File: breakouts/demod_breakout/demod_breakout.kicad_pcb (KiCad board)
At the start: 2 copper layers, 31 parts, among them P1 CONN_02X03, P2 CONN_01X02, U1 CONN_SMA, U2 mounting_box, U3 TCM-63AX+, U4 ADL5380, U5 TCM-63AX+, U6 CONN_SMA, U7 ADM7150

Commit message: demod component placement
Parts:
- added C21: 100 nF, Capacitors_SMD:C_0402, F.Cu at (91.0, 134.8)
- added C22: 100 nF, Capacitors_SMD:C_0402, F.Cu at (95.5, 110.0)
- added C23: 100 nF, Capacitors_SMD:C_0402, F.Cu at (93.2, 141.2)
- added C24: 100 nF, Capacitors_SMD:C_0402, F.Cu at (90.8, 102.0)
- added C25: DNP, Capacitors_SMD:C_0402, F.Cu at (96.2, 136.8)
- added C26: 100 nF, Capacitors_SMD:C_0402, F.Cu at (96.8, 141.8)
- added C27: DNP, Capacitors_SMD:C_0402, F.Cu at (88.2, 104.8)
- added C28: 100 nF, Capacitors_SMD:C_0402, F.Cu at (97.0, 105.5)
- added C29: 100 nF, Capacitors_SMD:C_0402, F.Cu at (103.8, 136.5)
- added C30: 100 nF, Capacitors_SMD:C_0402, F.Cu at (99.2, 98.0)
- added C31: 100 nF, Capacitors_SMD:C_0402, F.Cu at (104.8, 123.5)
- added C32: 100 nF, Capacitors_SMD:C_0402, F.Cu at (98.5, 131.0)
- added P3: CONN_02X03, Pin_Headers:Pin_Header_Straight_2x03, F.Cu at (111.5, 120.8)
- added P5: CONN_01X02, Pin_Headers:Pin_Header_Straight_1x02, F.Cu at (103.2, 127.8)
- added R10: 604, Resistors_SMD:R_0402, F.Cu at (90.2, 104.5)
- added R11: 604, Resistors_SMD:R_0402, F.Cu at (101.2, 136.8)
- added R12: 604, Resistors_SMD:R_0402, F.Cu at (95.8, 98.0)
- added R13: 0, Resistors_SMD:R_0402, F.Cu at (92.2, 138.8)
- added R14: 0, Resistors_SMD:R_0402, F.Cu at (90.2, 107.5)
- added R3: 10k, Resistors_SMD:R_0402, F.Cu at (89.2, 134.8)
- added R4: 10k, Resistors_SMD:R_0402, F.Cu at (95.2, 108.2)
- added R5: 10k, Resistors_SMD:R_0402, F.Cu at (91.2, 140.8)
- added R6: 10k, Resistors_SMD:R_0402, F.Cu at (92.5, 108.2)
- added R7: 604, Resistors_SMD:R_0402, F.Cu at (92.2, 136.8)
- added R8: 604, Resistors_SMD:R_0402, F.Cu at (88.2, 107.5)
- added R9: 604, Resistors_SMD:R_0402, F.Cu at (96.2, 138.8)
- added U10: LT1567, Housings_SSOP:MSOP-8_3x3mm_Pitch0.65mm, F.Cu at (101.2, 139.8)
- added U11: LT1567, Housings_SSOP:MSOP-8_3x3mm_Pitch0.65mm, F.Cu at (96.2, 101.0)
- added U12: CONN_SMA, vna_footprints:732512200_SMA, F.Cu at (111.2, 139.0)
- added U13: CONN_SMA, vna_footprints:732512200_SMA, F.Cu at (107.2, 100.0)
- added U14: LD1117S12CTR, TO_SOT_Packages_SMD:SOT-23, F.Cu at (98.2, 127.8)
- added U8: LTC1566-1, Housings_SOIC:SOIC-8_3.9x4.9mm_Pitch1.27mm, F.Cu at (91.0, 129.0)
- added U9: LTC1566-1, Housings_SOIC:SOIC-8_3.9x4.9mm_Pitch1.27mm, F.Cu at (91.0, 113.2)
- C6: footprint Capacitors_SMD:C_0603 -> Capacitors_SMD:C_0402
- moved U2 104.8 mm to (230.2, 39.5)
- moved U6 73.8 mm to (83.5, 140.0), turned to 90 degrees
- moved C3 72.0 mm to (78.5, 122.0), turned to 90 degrees
- moved C13 71.2 mm to (83.5, 134.0), turned to 270 degrees
- moved C5 70.6 mm to (80.0, 122.0), turned to 90 degrees
- moved U5 69.5 mm to (83.5, 129.5), turned to 180 degrees
- moved C9 68.5 mm to (83.0, 125.0), turned to 270 degrees
- moved C4 67.9 mm to (81.5, 116.0)
- moved C2 67.6 mm to (81.5, 114.0)
- moved C8 67.1 mm to (84.5, 125.0), turned to 270 degrees
- moved U4 66.5 mm to (83.8, 120.0)
- moved C6 65.6 mm to (83.5, 113.5), turned to 90 degrees
- moved U1 65.4 mm to (83.5, 98.0), turned to 270 degrees
- moved U3 65.1 mm to (83.5, 108.5)
- moved C1 65.0 mm to (83.5, 104.0), turned to 90 degrees
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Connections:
- P1 pad 1: /BRF_IN -> /ILO_ADL
- P1 pad 2: /BRF_IP -> /IHI_ADL
- P1 pad 5: /BRF_QN -> /QLO_ADL
- P1 pad 6: /BRF_QP -> /QHI_ADL
- U4 pad 21: Net-(C6-Pad1) -> Net-(C7-Pad1)
- U4 pad 22: Net-(C7-Pad1) -> Net-(C6-Pad1)
- U5 pad 2: GND -> Net-(C13-Pad1)
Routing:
- net GND: track 0.00 -> 25.6 mm, vias 0 -> 11
- net +5V: track 0.00 -> 11.0 mm
- net Net-(C1-Pad2): track 0.00 -> 5.45 mm
- net Net-(C13-Pad2): track 0.00 -> 5.45 mm
- net Net-(C7-Pad1): track 0.00 -> 4.41 mm
- net Net-(C6-Pad1): track 0.00 -> 4.00 mm
- net Net-(C6-Pad2): track 0.00 -> 3.39 mm
- net Net-(C7-Pad2): track 0.00 -> 2.96 mm
- net Net-(C9-Pad1): track 0.00 -> 2.71 mm
- net Net-(C8-Pad1): track 0.00 -> 2.71 mm
- net Net-(C9-Pad2): track 0.00 -> 2.68 mm
- net Net-(C8-Pad2): track 0.00 -> 2.47 mm
- net Net-(C1-Pad1): track 0.00 -> 2.36 mm
- net Net-(C13-Pad1): track 0.00 -> 2.36 mm
- added copper zone on In1.Cu, net GND
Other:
- board outline added: 40.8 x 50 mm
- copper layers 2 -> 4

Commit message: layout of demod board
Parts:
- moved P3 10.1 mm to (107.0, 129.8), turned to 180 degrees
- moved C30 10.0 mm to (89.2, 98.0)
- moved C20 9.20 mm to (108.5, 110.8)
- moved U7 9.02 mm to (103.8, 109.2)
- moved C18 8.84 mm to (107.0, 110.8)
- moved R2 8.84 mm to (107.0, 108.2)
- moved C19 8.66 mm to (106.5, 105.0)
- moved C12 8.55 mm to (100.0, 108.8)
- moved C14 8.38 mm to (99.2, 105.5)
- moved C15 8.36 mm to (98.2, 108.8)
- moved C17 8.05 mm to (100.2, 111.8)
- moved C16 7.97 mm to (102.5, 105.0)
- moved P5 7.81 mm to (104.2, 120.0), turned to 90 degrees
- moved C29 6.27 mm to (97.5, 137.0), turned to 0 degrees
- moved U12 6.05 mm to (105.2, 139.8), turned to 90 degrees
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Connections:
- P2 pad 1: Net-(C19-Pad2) -> GND
- P2 pad 2: GND -> Net-(C19-Pad2)
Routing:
- net /QHI_ADL: track 0.00 -> 18.8 mm
- net /QLO_ADL: track 0.00 -> 18.8 mm
- net /IHI_ADL: track 0.00 -> 13.5 mm, vias 0 -> 1
- net /ILO_ADL: track 0.00 -> 8.82 mm, vias 0 -> 1
- net Net-(C22-Pad1): track 0.00 -> 5.93 mm
- net Net-(C21-Pad1): track 0.00 -> 5.93 mm
- net GND: track 25.6 -> 30.0 mm, vias 11 -> 14
- net Net-(R1-Pad2): track 0.00 -> 1.78 mm
- net +5V: track 11.0 -> 11.8 mm, vias 0 -> 1
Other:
- board size 40.8 x 50 mm -> 33.8 x 50.2 mm

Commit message: layout of if processing on demodo board..
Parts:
- moved P5 9.52 mm to (106.5, 129.2), turned to 270 degrees
- moved C24 7.62 mm to (92.5, 107.2), turned to 270 degrees
- moved P3 6.52 mm to (106.5, 123.2)
- moved C31 5.01 mm to (99.8, 131.0), turned to 90 degrees
- moved R12 4.14 mm to (90.0, 101.0), turned to 270 degrees
- moved C30 3.40 mm to (92.0, 96.0), turned to 270 degrees
- moved R11 3.34 mm to (96.8, 138.0), turned to 180 degrees
- moved U14 3.34 mm to (97.0, 131.5)
- moved R5 3.26 mm to (89.8, 136.8), turned to 180 degrees
- moved C32 3.09 mm to (97.0, 134.2)
- moved C23 3.04 mm to (89.5, 138.2), turned to 0 degrees
- moved R9 2.69 mm to (94.5, 138.0), turned to 180 degrees
- moved C21 2.61 mm to (88.2, 135.0), turned to 180 degrees
- moved C27 2.37 mm to (89.0, 104.2), turned to 90 degrees
- moved R10 2.37 mm to (90.5, 104.2), turned to 90 degrees
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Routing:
- net /IOUT: track 0.00 -> 23.9 mm, vias 0 -> 1
- net +5V: track 11.8 -> 32.2 mm, vias 1 -> 7
- net /QOUT: track 0.00 -> 16.8 mm, vias 0 -> 1
- net /ILO_ADL: track 8.82 -> 21.9 mm, vias 1 -> 2
- net Net-(C27-Pad1): track 0.00 -> 12.9 mm
- net Net-(R13-Pad2): track 0.00 -> 12.2 mm, vias 0 -> 2
- net GND: track 30.0 -> 41.8 mm, vias 14 -> 26
- net Net-(C25-Pad1): track 0.00 -> 10.5 mm
- net /IHI_ADL: track 13.5 -> 23.8 mm, vias 1 -> 2
- net Net-(R14-Pad2): track 0.00 -> 9.76 mm, vias 0 -> 2
- net Net-(C22-Pad1): track 5.93 -> 11.8 mm
- net Net-(C21-Pad1): track 5.93 -> 11.8 mm
- net /VOUT_REF: track 0.00 -> 5.35 mm
- net Net-(R12-Pad1): track 0.00 -> 4.50 mm
- net Net-(R11-Pad1): track 0.00 -> 3.96 mm
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- added copper zone on In2.Cu, net +5V
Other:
- board text added: "IF I"
- board text added: "IF Q"
- board text added: "LO X dBm"
- board text added: "RF X dBm"
- board text added: "gnd 5v"
- board text added: "vref gnd"

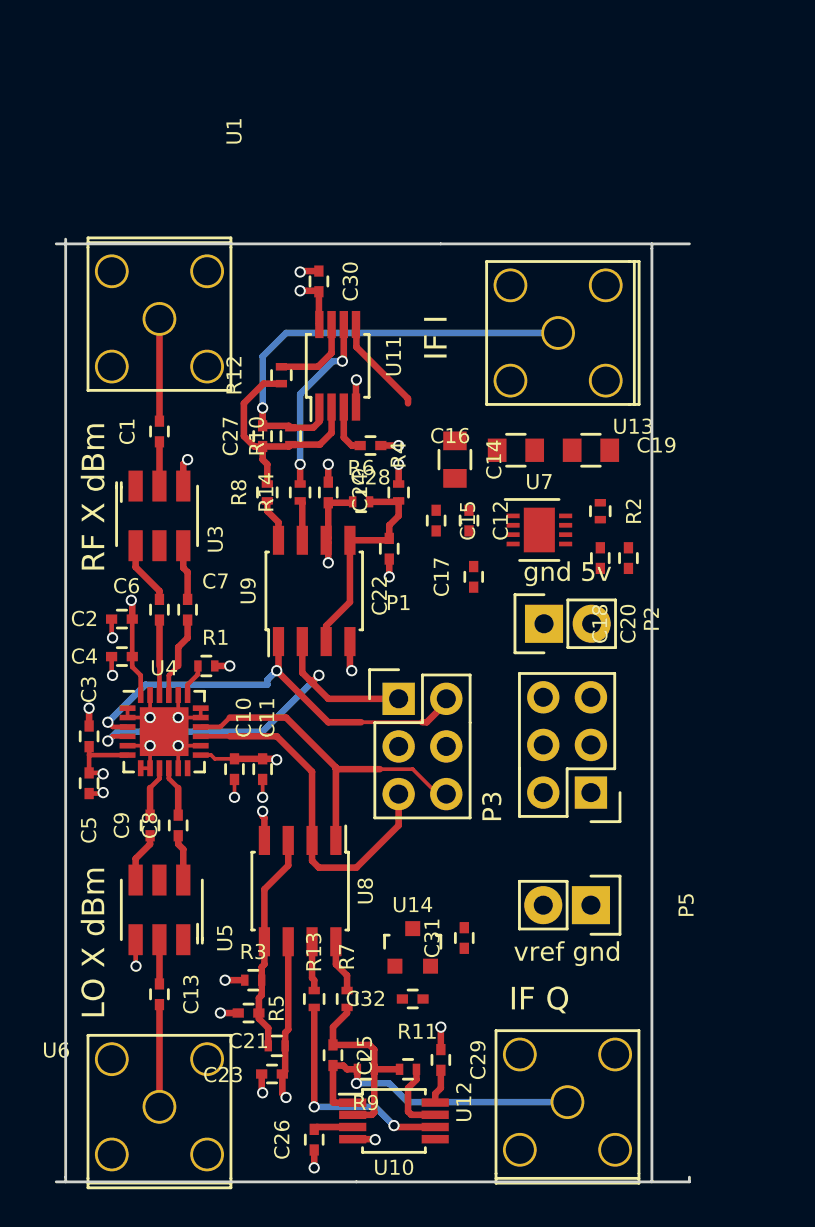
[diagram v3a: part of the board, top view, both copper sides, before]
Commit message: silkscreen cleanup on demod board
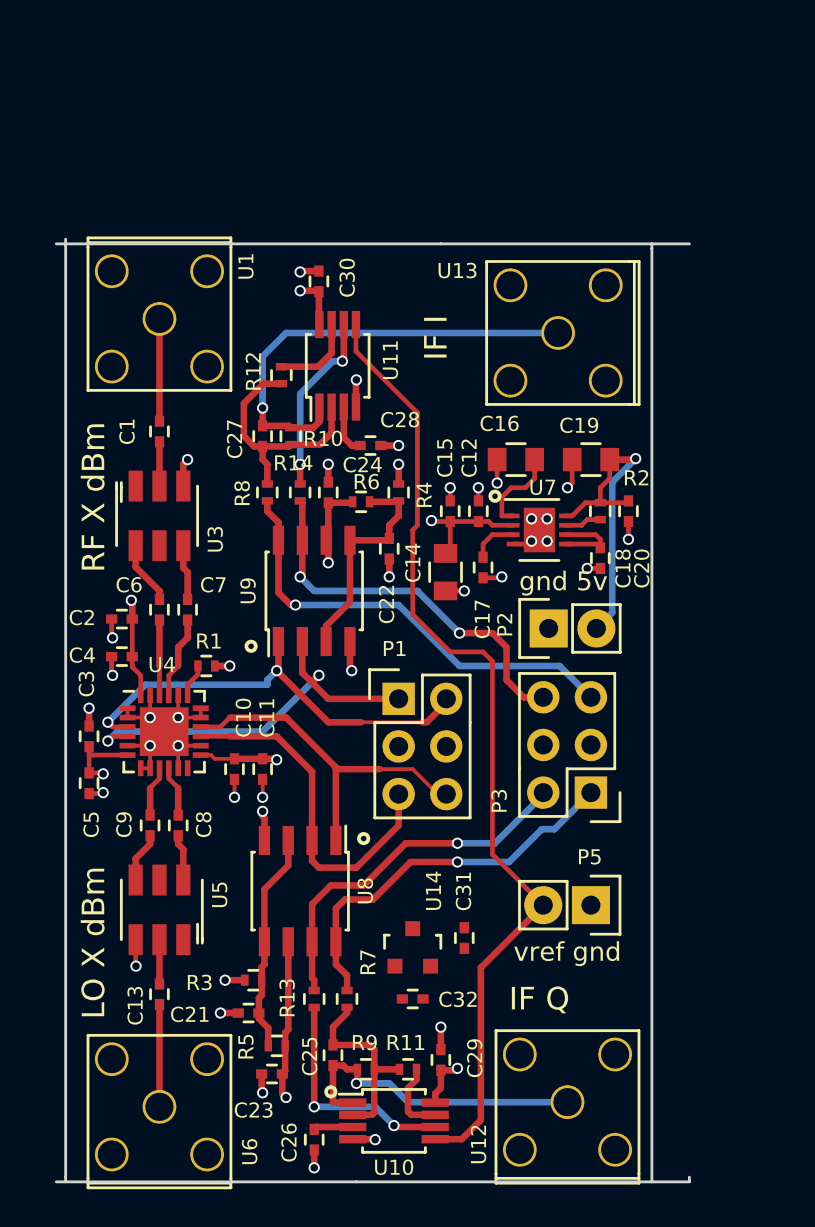
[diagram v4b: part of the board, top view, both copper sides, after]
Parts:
- moved C14 6.02 mm to (98.8, 111.5), turned to 90 degrees
- moved C20 2.50 mm to (108.5, 108.2)
- moved C15 0.90 mm to (99.0, 108.2)
- moved C12 0.71 mm to (100.5, 108.2)
- moved C17 0.71 mm to (100.8, 111.2)
- moved C16 0.50 mm to (102.5, 105.5)
- moved C19 0.50 mm to (106.5, 105.5)
- moved P2 0.35 mm to (104.2, 114.5)
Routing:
- net /VOUT_REF: track 5.35 -> 52.0 mm
- net /IIN1: track 2.35 -> 24.1 mm, vias 0 -> 1
- net /IIN2: track 2.15 -> 20.8 mm, vias 0 -> 2
- net /QIN1: track 2.98 -> 20.9 mm, vias 0 -> 1
- net Net-(C19-Pad2): track 0.00 -> 17.5 mm, vias 0 -> 1
- net /QIN2: track 2.65 -> 19.5 mm, vias 0 -> 1
- net GND: track 41.8 -> 51.5 mm, vias 26 -> 38
- net +5V: track 32.2 -> 39.4 mm, vias 7 -> 9
- net Net-(C16-Pad2): track 0.00 -> 4.76 mm
- net Net-(C18-Pad2): track 0.00 -> 4.34 mm
- net Net-(C17-Pad2): track 0.00 -> 2.51 mm
- net Net-(R2-Pad2): track 0.00 -> 1.97 mm
